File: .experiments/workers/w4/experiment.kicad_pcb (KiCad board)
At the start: 2 copper layers, 140 x 90 mm, 39 parts, among them J1 USB_C, J2 Output, J3 Debug, Q1 FS8205A, U1 USBLC6-2SC6, U2 BQ24072, U3 HY2113-KB5B, U4 MT3608, U5 AP2112K-3.3, U6 LN61CN3302MR-G

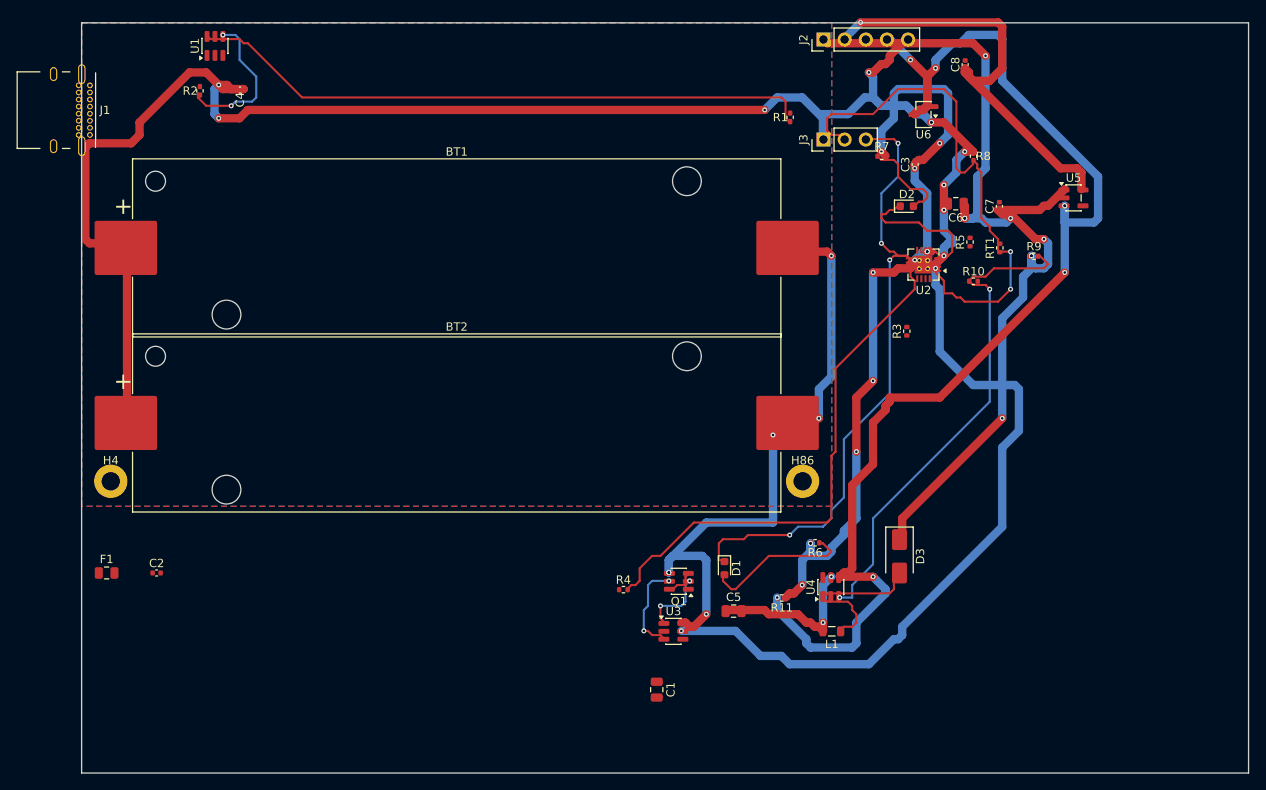
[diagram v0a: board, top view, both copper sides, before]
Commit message: 35-round experiment: best score 25.33, improved routing params
Router and conflict resolution tuning from autonomous optimization loop.
Best config: clearance=0.2051mm, cooling_factor=0.9735, existing_trace_cost=200.0

Co-Authored-By: Claude Opus 4.6 <noreply@anthropic.com>
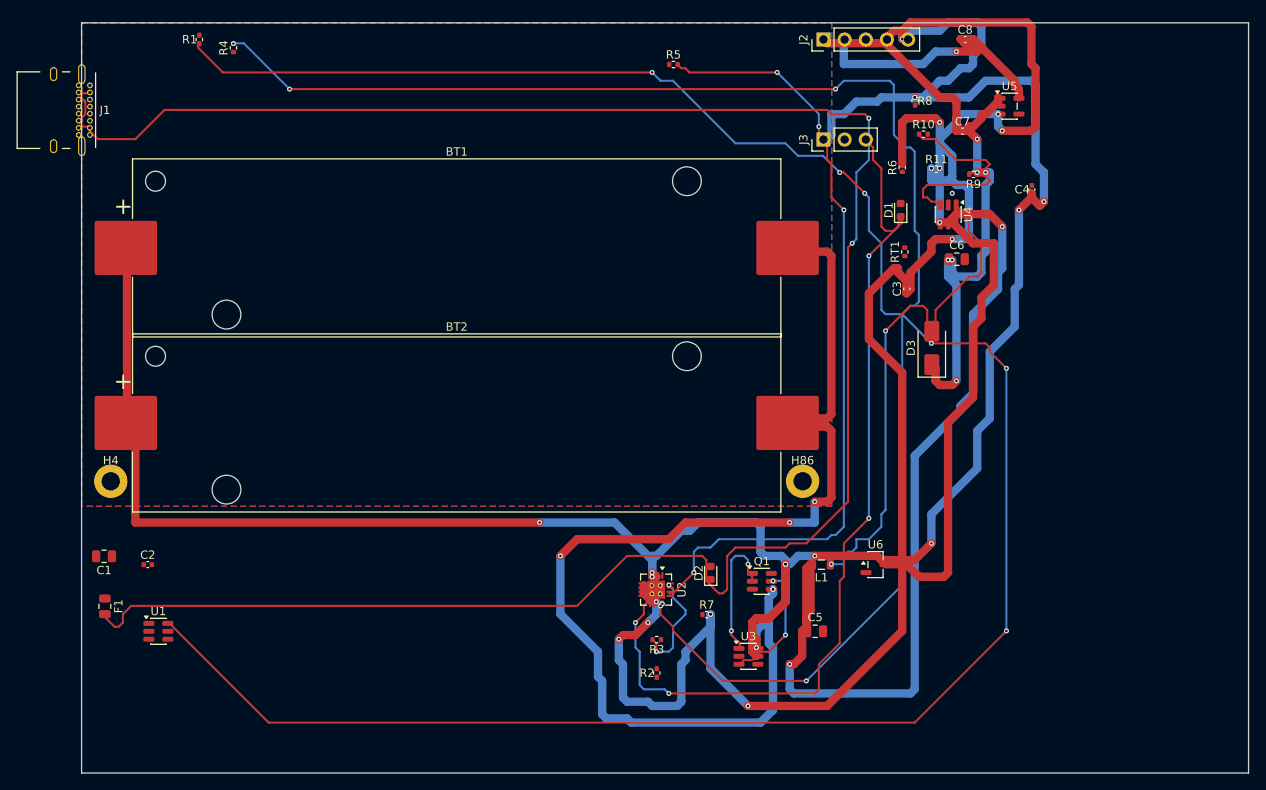
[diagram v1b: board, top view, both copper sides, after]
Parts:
- moved C4 95.7 mm to (114.0, 20.0), turned to 90 degrees
- moved R2 88.8 mm to (69.0, 78.0)
- moved R4 80.1 mm to (18.2, 3.00), turned to 90 degrees
- moved R1 71.5 mm to (14.1, 2.00)
- moved U1 70.6 mm to (9.21, 73.0), turned to 0 degrees
- moved C1 68.2 mm to (2.69, 64.0), turned to 180 degrees
- moved R7 58.9 mm to (75.0, 71.0)
- moved R11 54.7 mm to (102.5, 17.5), turned to 0 degrees
- moved U6 54.3 mm to (95.2, 65.0), turned to 0 degrees
- moved U2 50.5 mm to (68.9, 68.0), turned to -90 degrees
- moved D2 49.9 mm to (75.5, 66.0), turned to 90 degrees
- moved D1 47.9 mm to (98.3, 22.5), turned to 90 degrees
- moved R3 47.6 mm to (69.0, 74.0), turned to 180 degrees
- moved U4 46.9 mm to (104.0, 23.0), turned to -90 degrees
- moved R6 46.2 mm to (98.5, 17.4), turned to 90 degrees
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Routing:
- net Net-(F1-Pad2): track 0.00 -> 254.0 mm, vias 0 -> 2
- net Net-(R1-Pad1): track 75.5 -> 262.3 mm, vias 0 -> 6
- net Net-(U2-ILIM): track 62.7 -> 183.4 mm, vias 0 -> 6
- net Net-(U2-TMR): track 0.00 -> 96.0 mm, vias 0 -> 5
- net /VSYS_BOOST: track 19.4 -> 107.3 mm
- net /VSYS: track 93.0 -> 167.4 mm, vias 12 -> 10
- net /CELL_NEG: track 75.5 -> 147.0 mm
- net /NTC_SENSE: track 62.8 -> 0.00 mm, vias 2 -> 0
- net Net-(D3-A): track 19.7 -> 61.5 mm, vias 0 -> 2
- net /5V: track 115.5 -> 76.6 mm, vias 8 -> 6
- net /EN: track 149.0 -> 113.3 mm, vias 8 -> 6
- net /CHG_N: track 75.4 -> 108.5 mm
- net Net-(U4-FB): track 60.0 -> 27.6 mm, vias 2 -> 0
- net Net-(D2-K): track 18.7 -> 0.00 mm
- net /3V3: track 52.5 -> 34.0 mm
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
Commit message: 45-round experiment: best score 25.66, all nets routed (26/26)
Fixed A* performance by increasing max_search from 100k->500k to handle
high trace costs (100.0) without timing out. Kept high cost + coarse grid
(0.5mm) to prevent shorts while still routing efficiently.

Best config: edge_margin=5.7493mm, cooling_factor=0.9764, existing_trace_cost=200, max_rips=8

Co-Authored-By: Claude Opus 4.6 <noreply@anthropic.com>
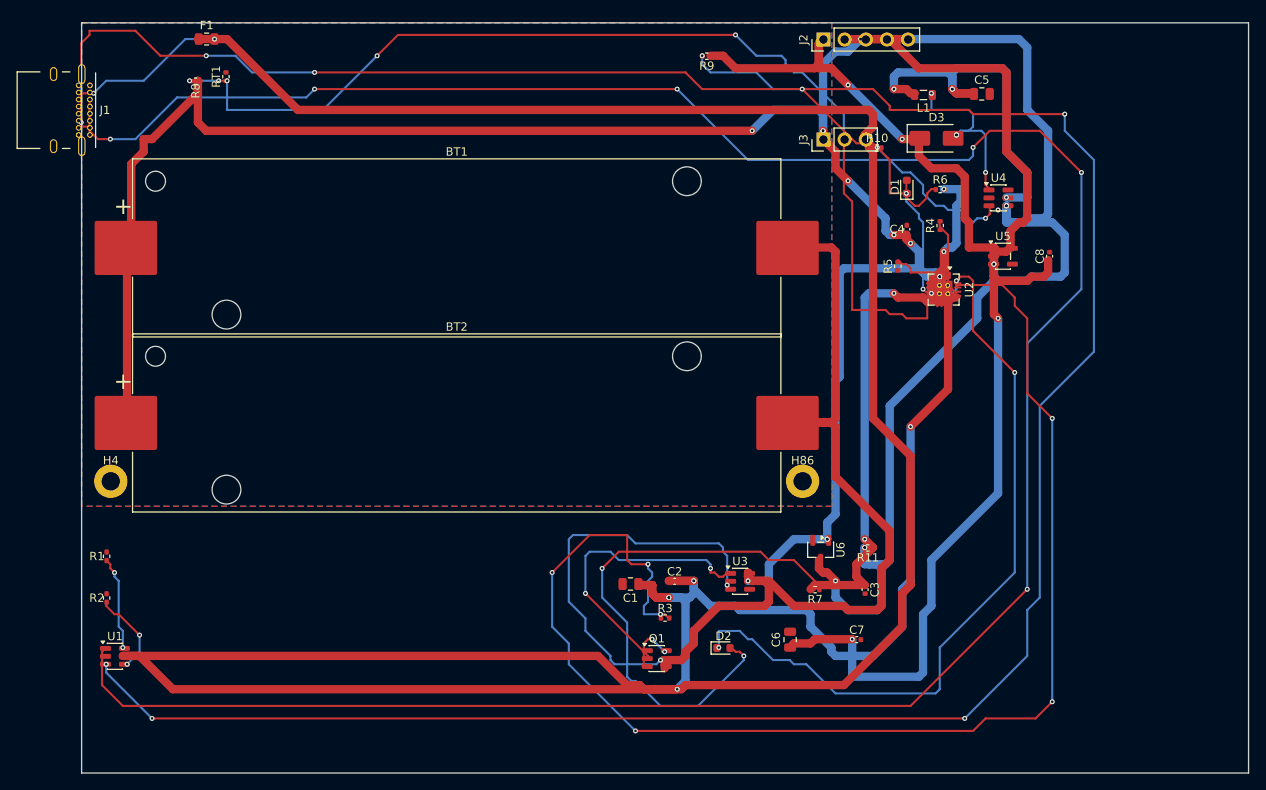
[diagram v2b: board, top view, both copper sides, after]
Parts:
- moved R4 87.4 mm to (103.0, 24.3)
- moved R8 86.3 mm to (13.7, 7.00), turned to 180 degrees
- moved RT1 84.1 mm to (17.3, 6.46)
- moved F1 69.1 mm to (15.0, 1.94), turned to 0 degrees
- moved C5 67.5 mm to (108.0, 8.53)
- moved R2 66.6 mm to (3.00, 69.0)
- moved C1 63.2 mm to (65.8, 67.3)
- moved C2 63.2 mm to (71.2, 67.0)
- moved R1 63.0 mm to (3.00, 64.0)
- moved C7 62.3 mm to (93.0, 74.0)
- moved L1 57.7 mm to (101.0, 8.66)
- moved U2 49.9 mm to (103.4, 32.0)
- moved C6 49.8 mm to (85.0, 74.0), turned to 90 degrees
- moved R11 46.2 mm to (94.3, 63.0), turned to 180 degrees
- moved C3 36.4 mm to (94.0, 68.0), turned to -90 degrees
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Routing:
- net /VBUS: track 0.00 -> 423.4 mm, vias 0 -> 6
- net Net-(J1-CC2): track 0.00 -> 319.5 mm, vias 0 -> 8
- net Net-(J1-CC1): track 0.00 -> 308.8 mm, vias 0 -> 6
- net Net-(R1-Pad1): track 262.3 -> 11.3 mm, vias 6 -> 2
- net Net-(F1-Pad2): track 254.0 -> 23.7 mm
- net Net-(U2-ILIM): track 183.4 -> 9.91 mm, vias 6 -> 0
- net Net-(U2-ISET): track 12.9 -> 159.0 mm, vias 2 -> 6
- net /NTC_SENSE: track 0.00 -> 129.3 mm, vias 0 -> 7
- net /VSYS: track 167.4 -> 70.6 mm, vias 10 -> 4
- net Net-(D2-K): track 0.00 -> 93.2 mm, vias 0 -> 4
- net Net-(U2-TMR): track 96.0 -> 8.95 mm, vias 5 -> 0
- net /CHG_N: track 108.5 -> 24.5 mm, vias 4 -> 2
- net Net-(D2-A): track 0.00 -> 63.4 mm, vias 0 -> 2
- net /VSYS_BOOST: track 107.3 -> 46.0 mm, vias 2 -> 4
- net /VBAT: track 289.7 -> 232.8 mm, vias 14 -> 12
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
